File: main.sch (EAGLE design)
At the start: 8 parts

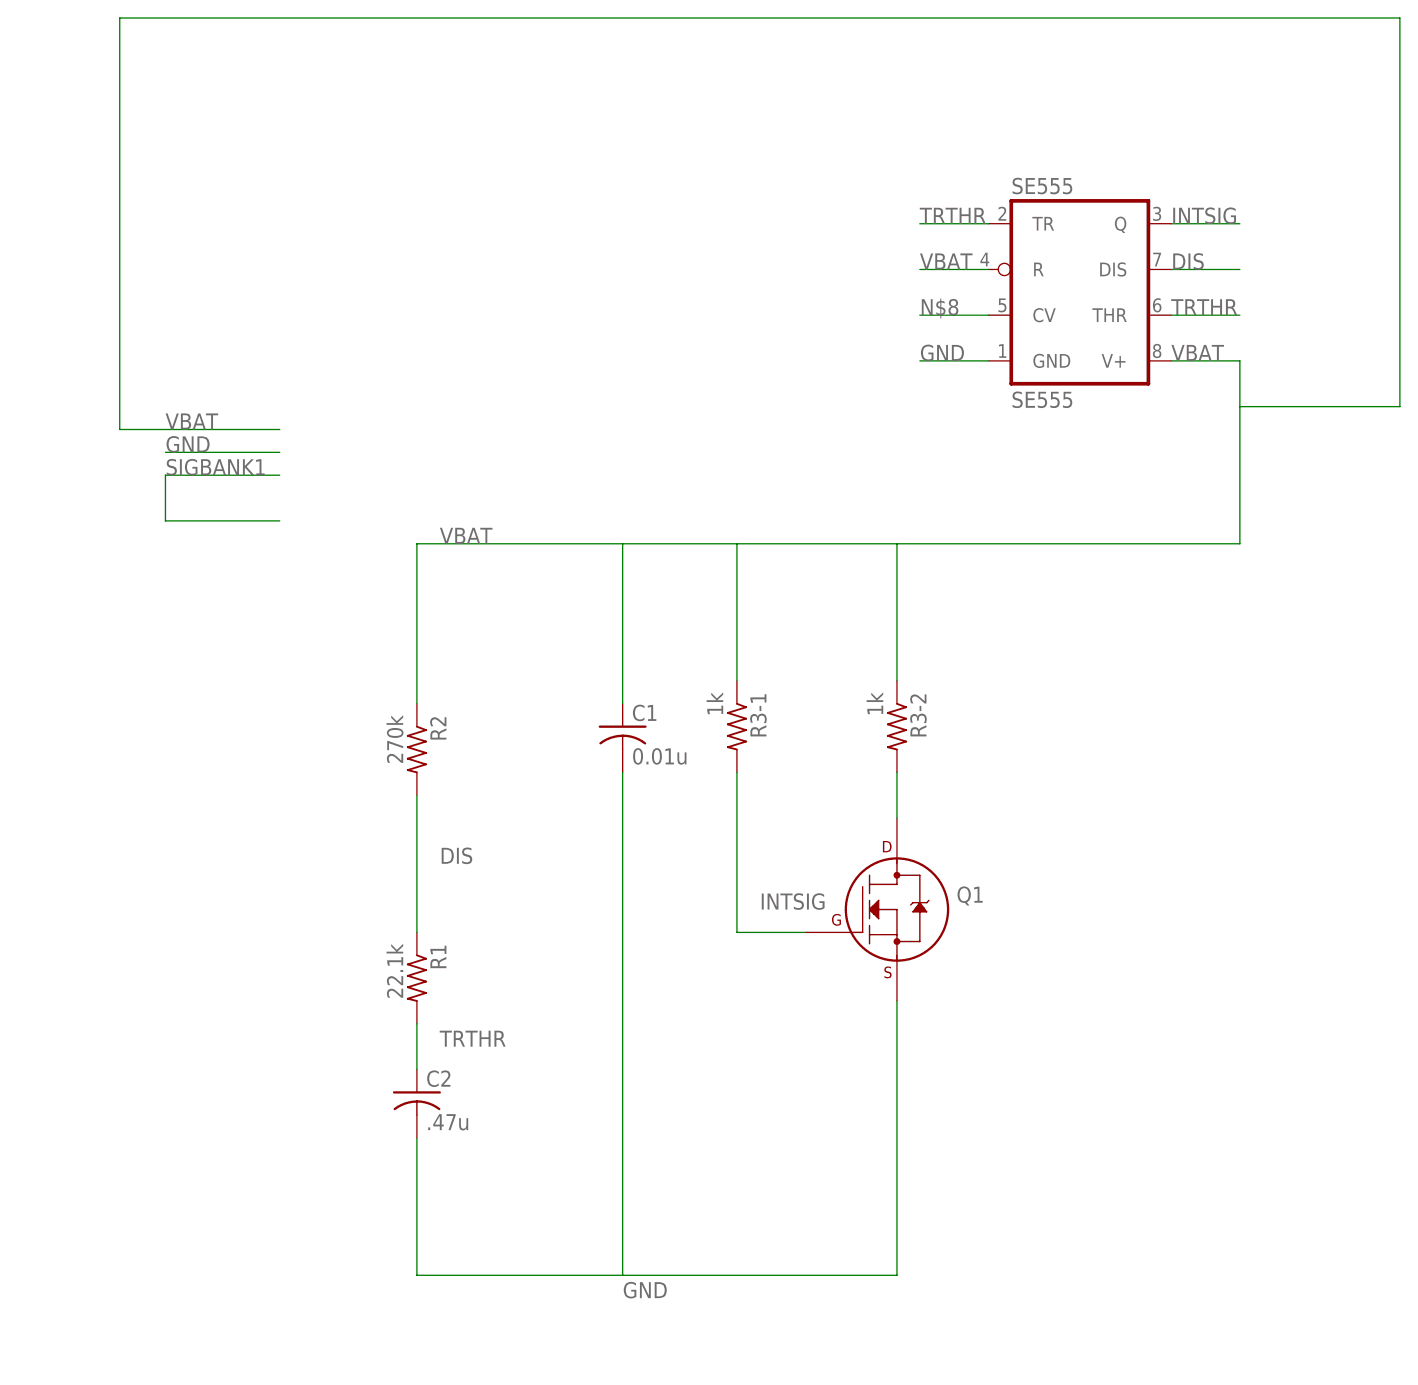
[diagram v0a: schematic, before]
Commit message: Corrections for pads
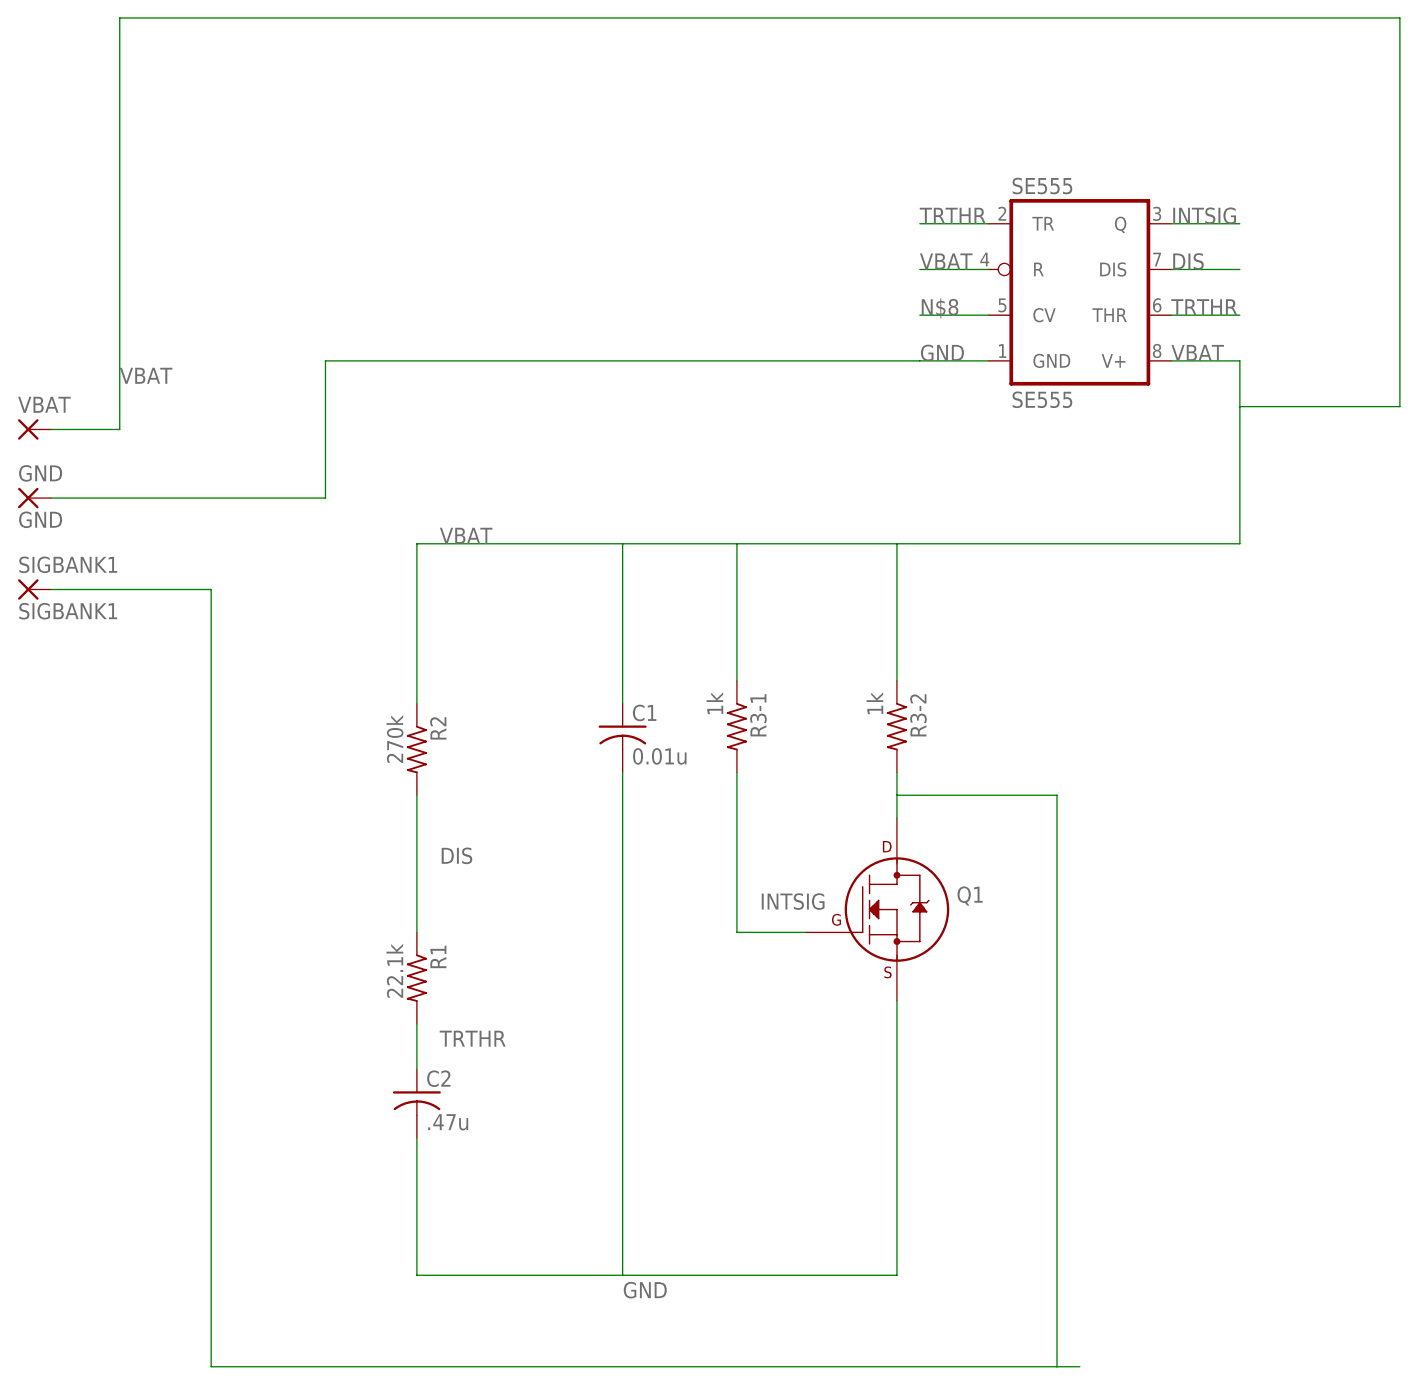
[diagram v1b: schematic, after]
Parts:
- added GND: GND, wirepad:3,17/1,3
- added SIGBANK1: SIGBANK1, wirepad:3,17/1,3
- added VBAT: (no value), wirepad:3,17/1,3
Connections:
- net GND: now also GND.P
- net SIGBANK1: now also SIGBANK1.P
- net VBAT: now also VBAT.P
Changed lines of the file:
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@@
 <layers>
 <layer number="1" name="Top" color="4" fill="1" visible="no" active="no"/>
+<layer number="2" name="Route2" color="1" fill="3" visible="no" active="no"/>
+<layer number="3" name="Route3" color="4" fill="3" visible="no" active="no"/>
+<layer number="14" name="Route14" color="1" fill="6" visible="no" active="no"/>
+<layer number="15" name="Route15" color="4" fill="6" visible="no" active="no"/>
 <layer number="16" name="Bottom" color="1" fill="1" visible="no" active="no"/>
 <layer number="17" name="Pads" color="2" fill="1" visible="no" active="no"/>
@@
 <part name="C2" library="adafruit" deviceset="C-US" device="C0805" value=".47u"/>
 <part name="C1" library="adafruit" deviceset="C-US" device="C0805" value="0.01u"/>
+<part name="VBAT" library="wirepad" deviceset="3,17/1,3" device=""/>
+<part name="GND" library="wirepad" deviceset="3,17/1,3" device="" value="GND"/>
+<part name="SIGBANK1" library="wirepad" deviceset="3,17/1,3" device="" value="SIGBANK1"/>
 </parts>
 <sheets>
@@
 <instance part="C2" gate="G$1" x="17.78" y="0"/>
 <instance part="C1" gate="G$1" x="40.64" y="40.64"/>
+<instance part="VBAT" gate="1" x="-25.4" y="73.66"/>
+<instance part="GND" gate="1" x="-25.4" y="66.04"/>
+<instance part="SIGBANK1" gate="1" x="-25.4" y="55.88"/>
 </instances>
 <busses>
@@
 <net name="VBAT" class="0">
 <segment>
-<wire x1="2.54" y1="73.66" x2="-15.24" y2="73.66" width="0.2032" layer="91"/>
+<wire x1="-22.86" y1="73.66" x2="-15.24" y2="73.66" width="0.2032" layer="91"/>
 <wire x1="-15.24" y1="73.66" x2="-15.24" y2="119.38" width="0.2032" layer="91"/>
 <wire x1="-15.24" y1="119.38" x2="127" y2="119.38" width="0.2032" layer="91"/>
@@
 <wire x1="109.22" y1="76.2" x2="109.22" y2="81.28" width="0.2032" layer="91"/>
 <wire x1="127" y1="76.2" x2="109.22" y2="76.2" width="0.2032" layer="91"/>
-<label x="-10.16" y="73.66" size="1.778" layer="95"/>
+<label x="-15.24" y="78.74" size="1.778" layer="95"/>
 <label x="20.32" y="60.96" size="1.778" layer="95"/>
 <label x="101.6" y="81.28" size="1.778" layer="95"/>
@@
 <pinref part="R3-1" gate="G$1" pin="1"/>
 <pinref part="SE555" gate="A" pin="V+"/>
+<pinref part="VBAT" gate="1" pin="P"/>
 </segment>
 <segment>
@@
 <net name="GND" class="0">
 <segment>
-<wire x1="2.54" y1="71.12" x2="-10.16" y2="71.12" width="0.2032" layer="91"/>
-<label x="-10.16" y="71.12" size="1.778" layer="95"/>
-</segment>
-<segment>
 <wire x1="81.28" y1="81.28" x2="73.66" y2="81.28" width="0.2032" layer="91"/>
 <label x="73.66" y="81.28" size="1.778" layer="95"/>
 <pinref part="SE555" gate="A" pin="GND"/>
+<wire x1="73.66" y1="81.28" x2="7.62" y2="81.28" width="0.1524" layer="91"/>
+<wire x1="7.62" y1="81.28" x2="7.62" y2="66.04" width="0.1524" layer="91"/>
+<pinref part="GND" gate="1" pin="P"/>
+<wire x1="7.62" y1="66.04" x2="-22.86" y2="66.04" width="0.1524" layer="91"/>
 </segment>
 <segment>
@@
 <net name="SIGBANK1" class="0">
 <segment>
-<wire x1="2.54" y1="68.58" x2="-10.16" y2="68.58" width="0.2032" layer="91"/>
-<wire x1="2.54" y1="63.5" x2="-10.16" y2="63.5" width="0.2032" layer="91"/>
-<wire x1="-10.16" y1="63.5" x2="-10.16" y2="68.58" width="0.2032" layer="91"/>
-<label x="-10.16" y="68.58" size="1.778" layer="95"/>
-</segment>
-<segment>
-<wire x1="71.12" y1="30.48" x2="71.12" y2="35.56" width="0.2032" layer="91"/>
+<wire x1="71.12" y1="30.48" x2="71.12" y2="33.02" width="0.2032" layer="91"/>
 <pinref part="Q1" gate="G$1" pin="D"/>
 <pinref part="R3-2" gate="G$1" pin="2"/>
+<pinref part="SIGBANK1" gate="1" pin="P"/>
+<wire x1="71.12" y1="33.02" x2="71.12" y2="35.56" width="0.2032" layer="91"/>
+<wire x1="-22.86" y1="55.88" x2="-5.08" y2="55.88" width="0.1524" layer="91"/>
+<wire x1="-5.08" y1="55.88" x2="-5.08" y2="-30.48" width="0.1524" layer="91"/>
+<wire x1="-5.08" y1="-30.48" x2="88.9" y2="-30.48" width="0.1524" layer="91"/>
+<wire x1="91.44" y1="-30.48" x2="88.9" y2="-30.48" width="0.1524" layer="91"/>
+<wire x1="88.9" y1="-30.48" x2="88.9" y2="33.02" width="0.1524" layer="91"/>
+<wire x1="88.9" y1="33.02" x2="71.12" y2="33.02" width="0.1524" layer="91"/>
 </segment>
 </net>
